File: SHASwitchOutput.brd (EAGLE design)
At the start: 47 x 64 mm, 39 parts, among them IC2 HLKPM01, Q1 2N7002, Q2 2N7002, Q3 2N7002, Q4 2N7002

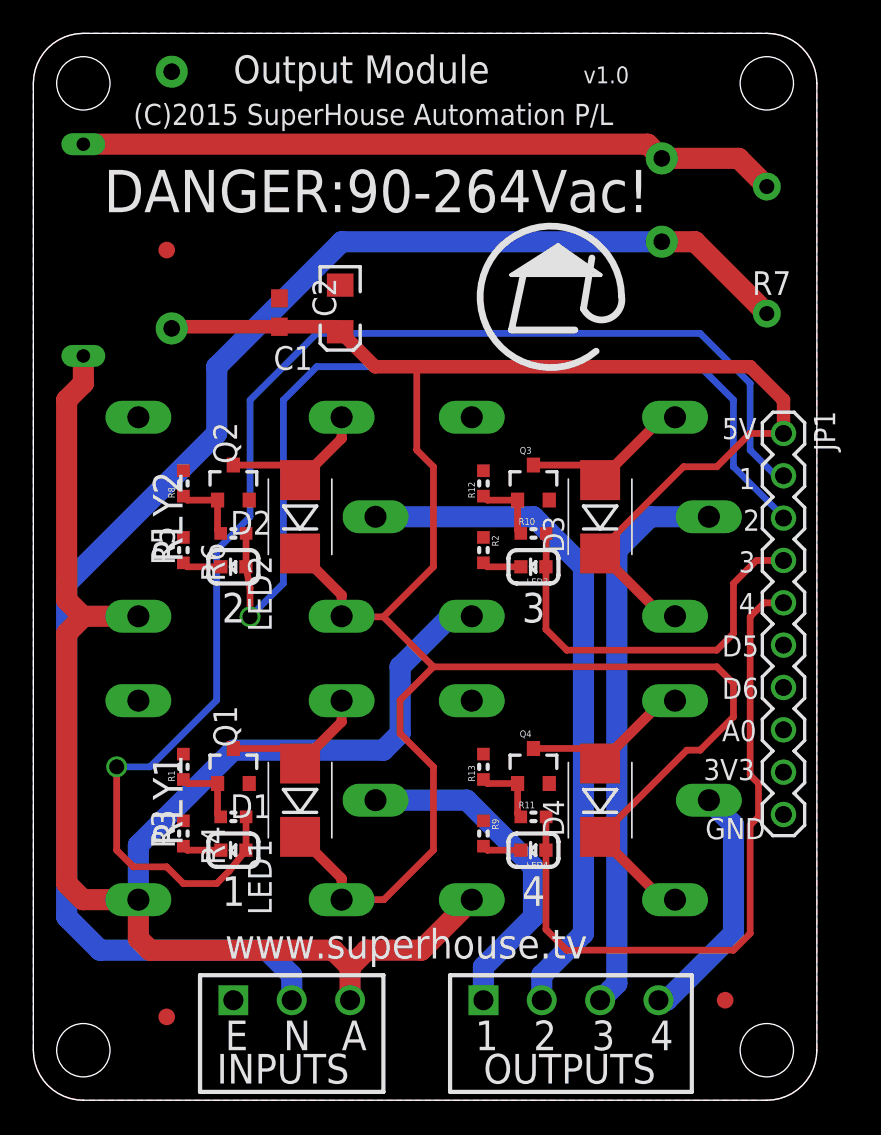
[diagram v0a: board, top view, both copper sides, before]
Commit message: Changed screw terminals from 3.5mm pitch to 5mm
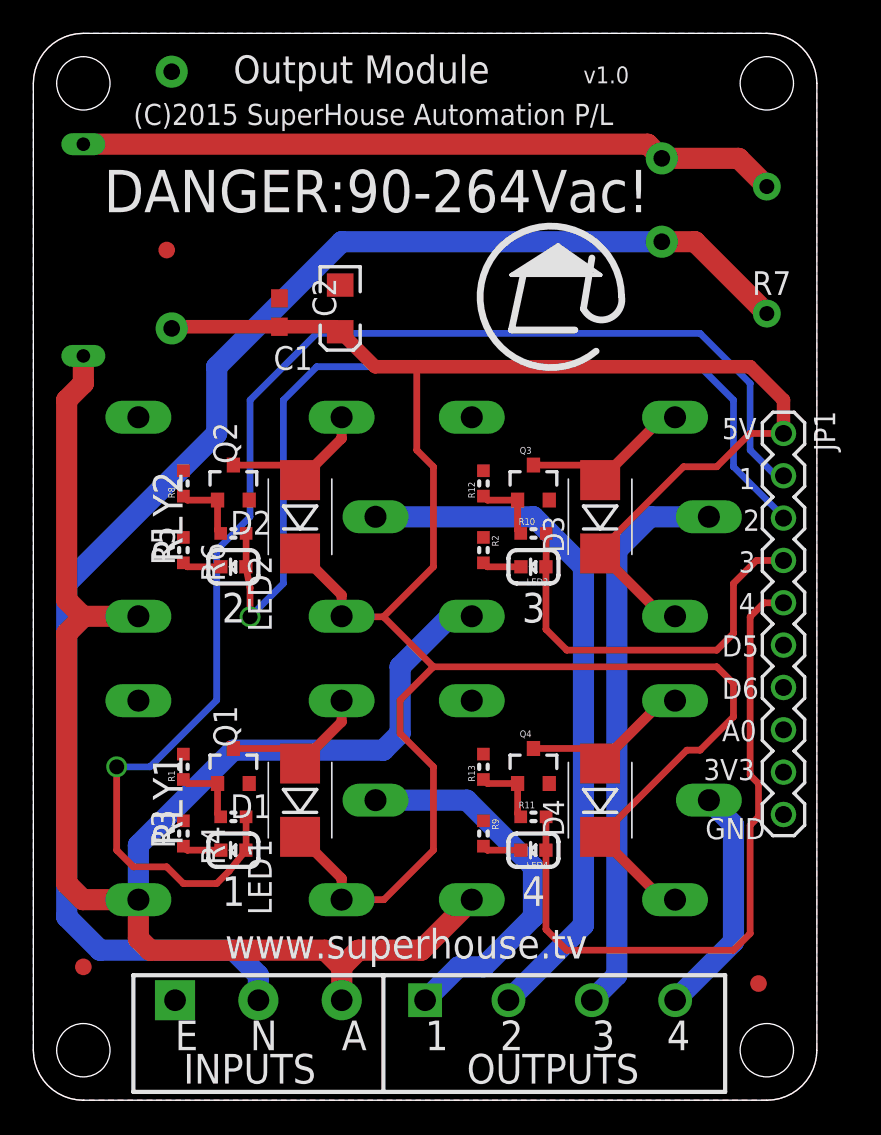
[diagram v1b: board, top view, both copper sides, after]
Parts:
- removed J1: (no value), freetronics-master-v1.1:SCREWTERMINAL-3.5MM-4
- added JP5: (no value), freetronics-jon:SCREWTERMINAL-5MM-4
- JP2: device freetronics-original:SCREWTERMINAL-3.5MM-3 -> freetronics-jon:SCREWTERMINAL-5MM-3
- moved FID3 5.83 mm to (3.00, 8.00)
- moved JP2 3.50 mm to (8.50, 6.00)
- moved FID2 2.24 mm to (43.5, 7.00)
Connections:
- net ACTIVE1: now also JP5.1; no longer J1.1
- net ACTIVE2: now also JP5.2; no longer J1.2
- net ACTIVE3: now also JP5.3; no longer J1.3
- net ACTIVE4: now also JP5.4; no longer J1.4
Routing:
- net ACTIVE1: track 20.4 -> 22.7 mm
- net NEUTRAL: track 91.1 -> 89.1 mm
- net ACTIVE2: track 40.8 -> 41.6 mm
- net ACTIVE4: track 14.8 -> 14.1 mm
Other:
- board text added: "90 to 264V"
- board text removed: "90 to 264Vac"
